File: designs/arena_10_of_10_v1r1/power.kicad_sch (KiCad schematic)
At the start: 4 parts, among them J25 Barrel_Jack, J26 Barrel_Jack, SW1 SW_SPDT, U82 RB-XXYYD

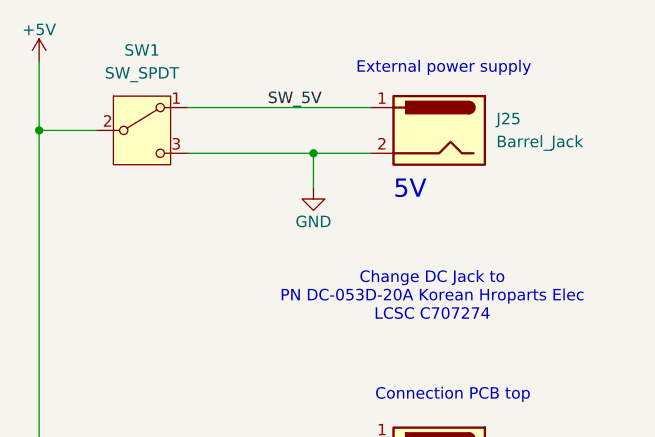
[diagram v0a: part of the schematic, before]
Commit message: disconnect SW1 pin 3
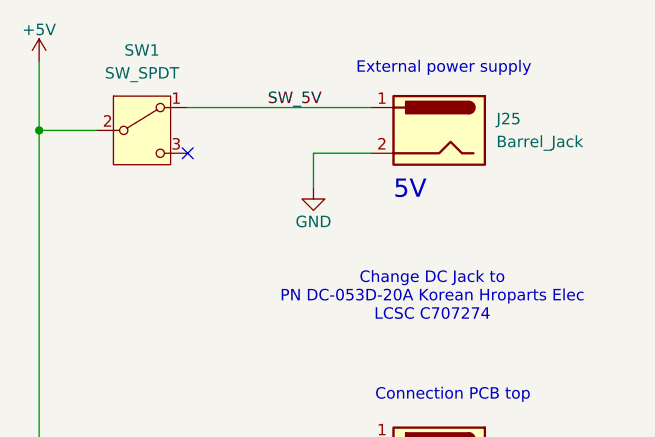
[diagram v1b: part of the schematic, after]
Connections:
- net GND: no longer SW1.3 (C)
- no-connect marks 0 -> 1
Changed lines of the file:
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@@
 		(title "G6 Teensy 10-10 Arena")
 		(date "2026-04-22")
-		(rev "v1.1.3")
+		(rev "v1.1.4")
 		(company "IORodeo for Reiser Lab @ Janelia | HHMI")
 	)
@@
 	)
 	(junction
-		(at 63.5 34.29)
-		(diameter 0)
-		(color 0 0 0 0)
-	)
-	(junction
 		(at 33.02 31.75)
 		(diameter 0)
@@
 		(diameter 0)
 		(color 0 0 0 0)
+	)
+	(no_connect
+		(at 49.53 34.29)
 	)
 	(wire
@@
 		)
 		(stroke
-			(width 0)
-			(type default)
-		)
-	)
-	(wire
-		(pts
-			(xy 49.53 34.29) (xy 63.5 34.29)
-		)
-		(stroke
